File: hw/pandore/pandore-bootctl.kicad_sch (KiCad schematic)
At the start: 0 parts

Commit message: most of board control signals added, routed and defined
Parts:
- added B1: PWR, megaxone_mechanical:TACT_PTS810, symbol megaxone_mechanical:Tact_NO
- added B2: RST, megaxone_mechanical:TACT_PTS810, symbol megaxone_mechanical:Tact_NO
- added C238, C239: ${Capacitance}, ${Voltage}, ${Dielectric}, reekilib_cap:CAPC1608, symbol reekilib_cap:cap
- added C258: ${Capacitance}, ${Voltage}, ${Dielectric}, reekilib_cap:CAPC2012, symbol reekilib_cap:cap
- added D32: ${Vr}, ${Io}, ${Vf}, reekilib_sod:sod-123, symbol reekilib_dio:diode
- added D34, D35: ${color}, reekilib_led:LEDM1608X80, symbol reekilib_led:led
- added J30: PWRBTN, reekilib_con:HDR254P1X02-TH, symbol reekilib_con:hdr-1x2
- added J31: RSTBTN, reekilib_con:HDR254P1X02-TH, symbol reekilib_con:hdr-1x2
- added JMP12: AUTOON, reekilib_con:HDR254P1X02-TH, symbol reekilib_con:hdr-1x2
- added Q11, Q12, Q13, Q14, Q15: MOSFET_EN-N, reekilib_sot:SOT95P280X100-3, symbol reekilib_mfe:MOSFET_EN-N
- added R209, R210, R217, R218, R219, R220, R221, R222, R229, R230: ${Resistance}, ${Tolerance}, ${Power}, reekilib_res:RESC1005, symbol reekilib_res:res
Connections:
- new net: C258.2, D32.2 (A), Q11.1 (G), R222.2
- new net: Q13.1 (G), R217.1, R218.2
- new net: B2.4, C239.2, J31.2, R210.1
- new net: Q11.3 (D), Q12.1 (G), R221.2
- new net: B1.4, C238.2, J30.2, R209.1
- new net: D34.C, R229.2
- new net: Q14.1 (G), R219.1, R220.2
- new net: Q14.2 (S), Q15.3 (D)
- new net: Q14.3 (D), R230.1
- new net: D35.C, R230.2
- new net: Q13.3 (D), Q15.1 (G), R229.1
- new net: JMP12.1, Q12.3 (D)
- new net PWRSW: JMP12.2, R209.2
- new net RSTSW: R210.2
- new net STATE0: R218.1
- new net STATE3: R220.1
- new net VSS: B1.1, B2.1, C238.1, C239.1, C258.1, J30.1, J31.1, Q11.2 (S), Q12.2 (S), Q13.2 (S), Q15.2 (S), R217.2, R219.2
- new net VSTBY: D32.1 (C), D34.A, D35.A, R221.1, R222.1

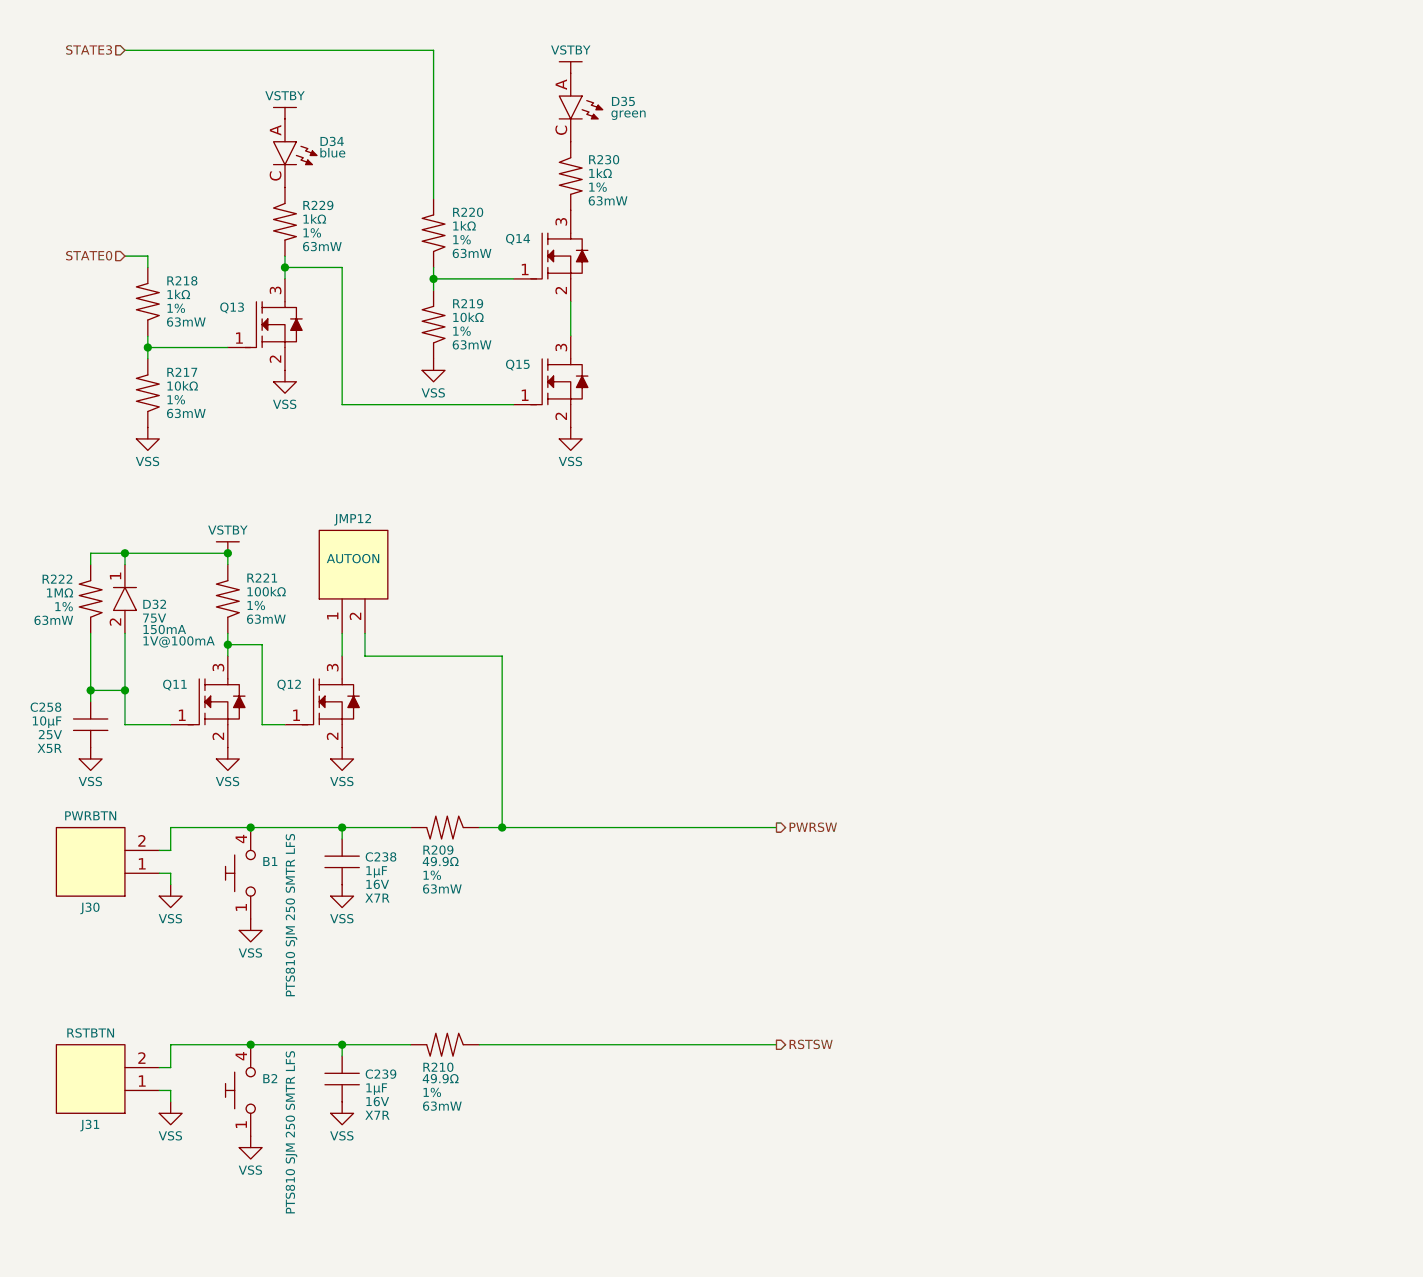
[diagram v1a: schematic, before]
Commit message: added expansion port and more ctl to rp2350s routing much progress
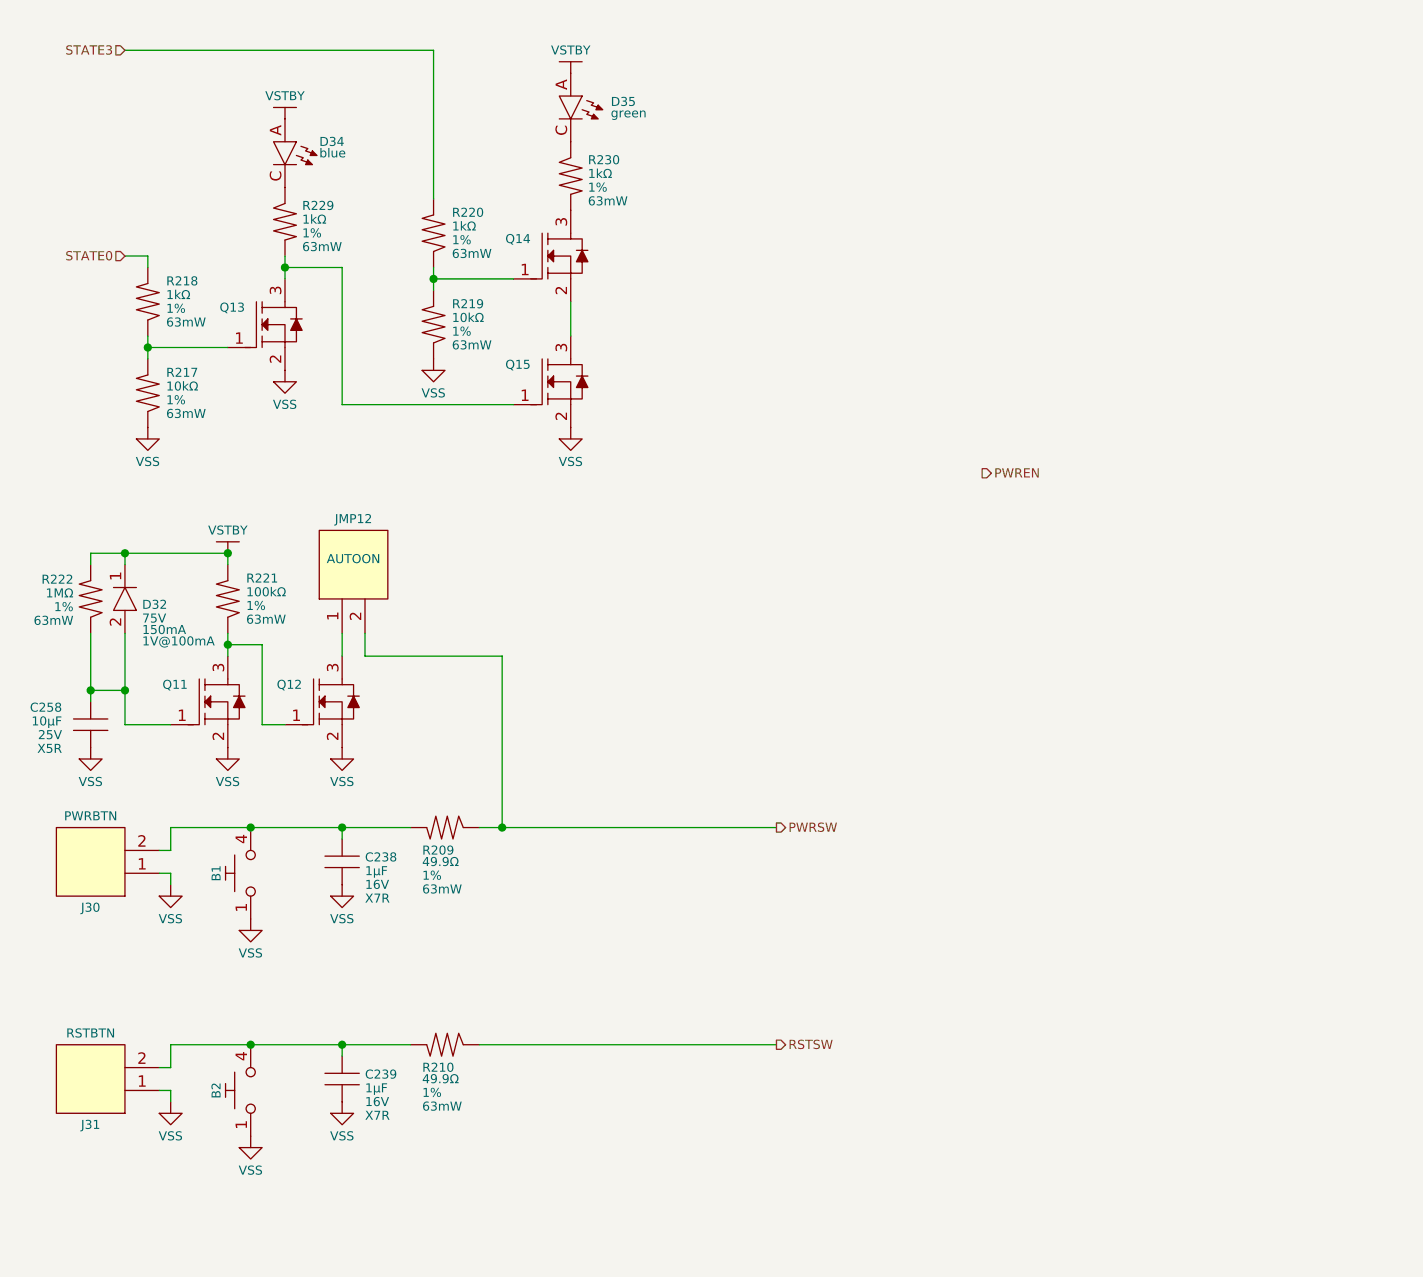
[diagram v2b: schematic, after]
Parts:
- removed B1: PWR, megaxone_mechanical:TACT_PTS810, symbol megaxone_mechanical:Tact_NO
- removed B2: RST, megaxone_mechanical:TACT_PTS810, symbol megaxone_mechanical:Tact_NO
- added B1, B2: mom_tact_no, reekilib_msw:tact_460X320X250, symbol reekilib_msw:mom_tact_no
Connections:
- net VSS: now also B1.1, B1.2, B2.1, B2.2
- net at C239.2, J31.2, R210.1: now also B2.3, B2.4
- net at C238.2, J30.2, R209.1: now also B1.3, B1.4

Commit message: more routing/placement done added 5v load switch 1A each added second fan circuit redone all diffpair routing following new stackup calc added all (?) missing connectors to unused pins
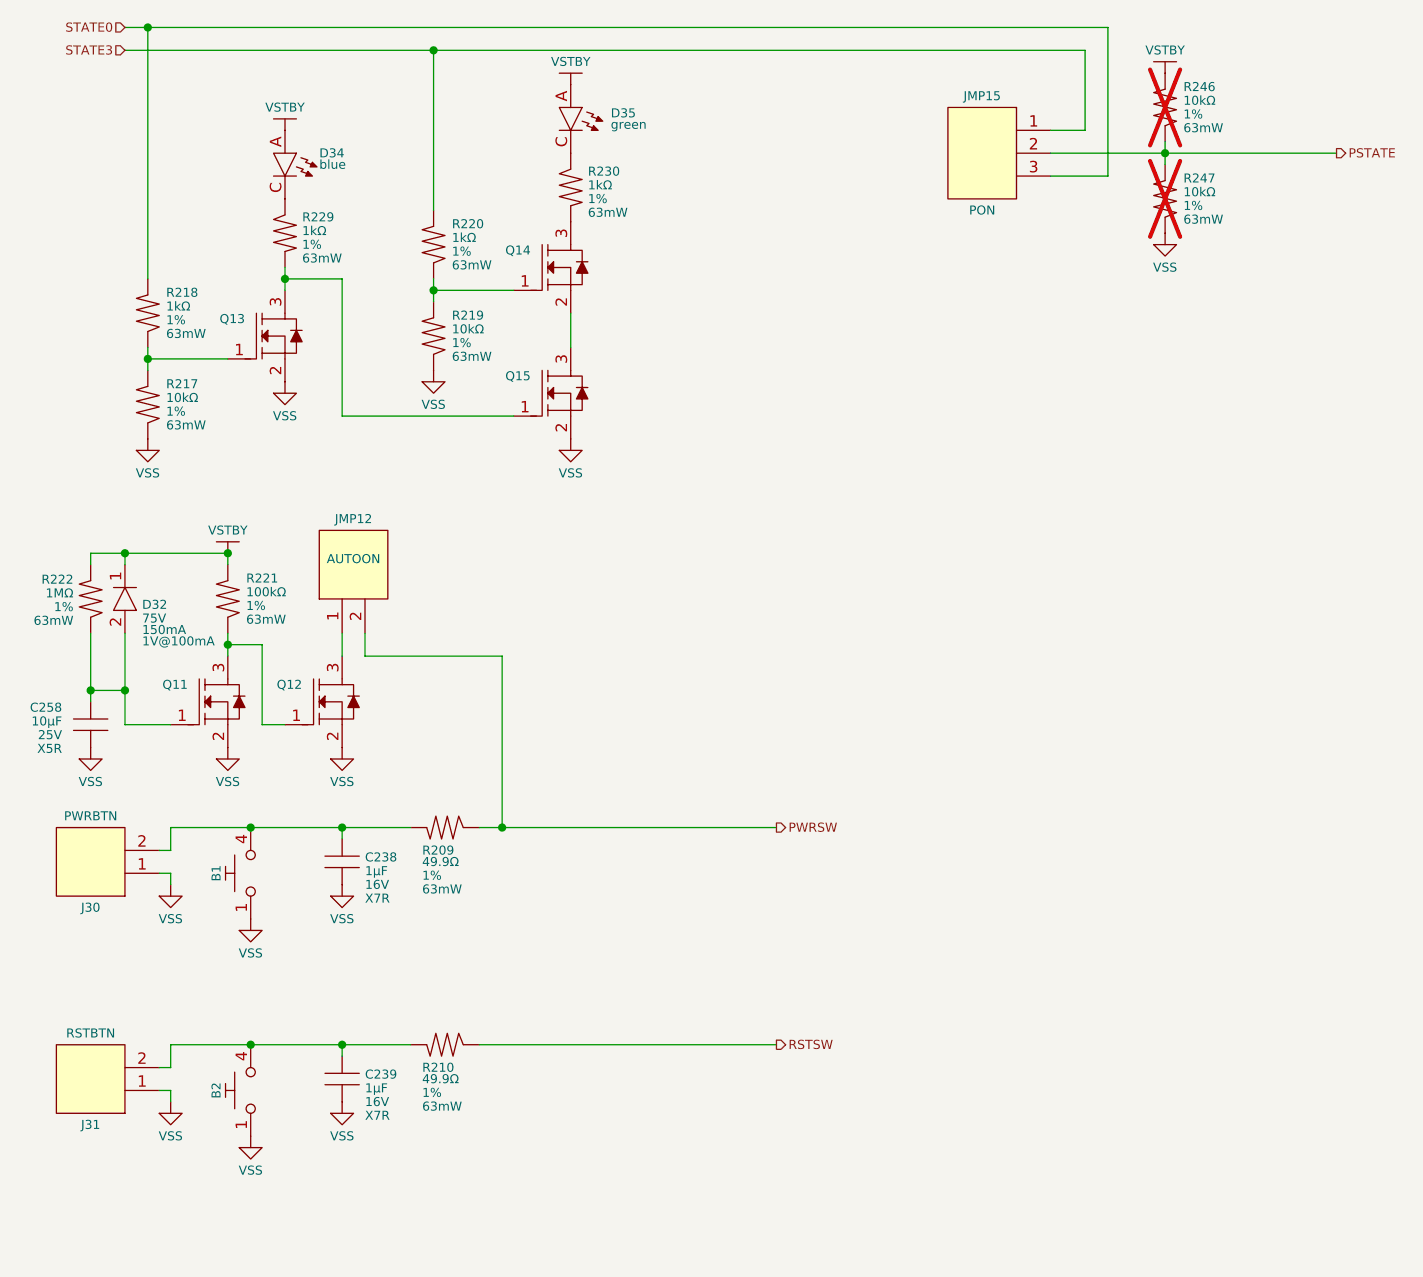
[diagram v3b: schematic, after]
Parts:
- added JMP15: PON, reekilib_con:HDR254P1X03-TH, symbol reekilib_con:hdr-1x3
- added R246, R247: ${Resistance}, ${Tolerance}, ${Power}, reekilib_res:RESC1005, symbol reekilib_res:res
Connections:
- net STATE0: now also JMP15.3
- net STATE3: now also JMP15.1
- net VSS: now also R247.2
- net VSTBY: now also R246.1
- new net PSTATE: JMP15.2, R246.2, R247.1
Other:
- moved on the sheet: D34, D35, Q13, Q14, Q15, R217, R218, R219, R220, R229, R230

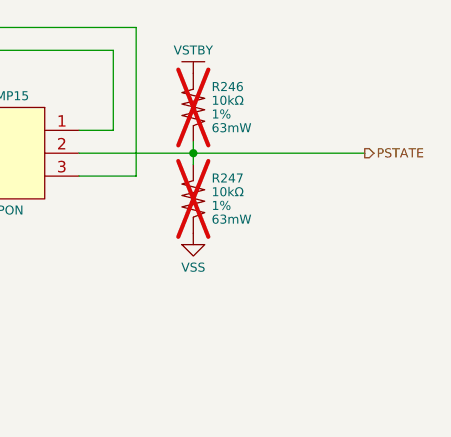
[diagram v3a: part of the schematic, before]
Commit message: added monitor amp with volume knob continue routing all around
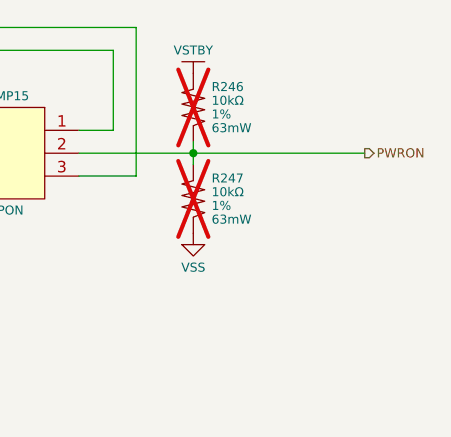
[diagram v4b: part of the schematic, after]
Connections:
- net PSTATE renamed PWRON
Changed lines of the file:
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@@
 		)
 	)
-	(hierarchical_label "PSTATE"
+	(hierarchical_label "PWRON"
 		(shape output)
 		(at 196.85 46.99 0)
